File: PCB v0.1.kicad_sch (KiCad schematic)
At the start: 59 parts, among them J1 XT60 M (Vertical), J10 2.54mm 3P, J11 2.54mm 3P, J12 2.54mm 3P, J13 JST-SH 3P, J14 JST-SH 3P, J15 JST-SH 3P, J16 JST-SH 3P, J17 JST-SH 3P, J18 JST-SH 3P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

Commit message: Rev A finished. docs made, BOM made.
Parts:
- U1: Taobao https://item.taobao.com/item.htm?id=535067252604&last_time=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 -> https://item.taobao.com/item.htm?id=635227665423&spm=a312a.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
- U2: Taobao https://item.taobao.com/item.htm?abbucket=6&id=562966932146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 -> https://item.taobao.com/item.htm?id=635227665423&spm=a312a.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
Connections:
- net BLDC_0: now also A1.14 (GPIO10); no longer A1.4 (GPIO2)
- net BLDC_1: now also A1.16 (GPIO12); no longer A1.6 (GPIO4)
- net BLDC_2: now also A1.19 (GPIO14); no longer A1.9 (GPIO6)
- net BLDC_4: now also A1.32 (GPIO27_ADC1); no longer A1.14 (GPIO10)
- net BLDC_5: now also A1.26 (GPIO20); no longer A1.16 (GPIO12)
- net ENC_0: now also A1.4 (GPIO2); no longer A1.21 (GPIO16)
- net ENC_1: now also A1.5 (GPIO3); no longer A1.22 (GPIO17)
- net ENC_2: now also A1.6 (GPIO4); no longer A1.24 (GPIO18)
- net ENC_3: now also A1.7 (GPIO5); no longer A1.25 (GPIO19)
- net ENC_4: now also A1.9 (GPIO6); no longer A1.26 (GPIO20)
- net ENC_5: now also A1.10 (GPIO7); no longer A1.27 (GPIO21)
- net REV_0: now also A1.15 (GPIO11); no longer A1.5 (GPIO3)
- net REV_1: now also A1.17 (GPIO13); no longer A1.7 (GPIO5)
- net REV_2: now also A1.20 (GPIO15); no longer A1.10 (GPIO7)
- net REV_4: now also A1.34 (GPIO28_ADC2); no longer A1.15 (GPIO11)
- net REV_5: now also A1.27 (GPIO21); no longer A1.17 (GPIO13)
- net SERVO_0: now also A1.21 (GPIO16); no longer A1.19 (GPIO14)
- net SERVO_1: now also A1.22 (GPIO17); no longer A1.20 (GPIO15)
- net SERVO_2: now also A1.24 (GPIO18); no longer A1.32 (GPIO27_ADC1)
- net SERVO_3: now also A1.25 (GPIO19); no longer A1.34 (GPIO28_ADC2)

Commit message: Created new layout, fixed XT30 polarity
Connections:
- net BLDC_0: now also A1.7 (GPIO5); no longer A1.14 (GPIO10)
- net BLDC_1: now also A1.14 (GPIO10); no longer A1.16 (GPIO12)
- net BLDC_2: now also A1.11 (GPIO8); no longer A1.19 (GPIO14)
- net BLDC_3: now also A1.9 (GPIO6); no longer A1.11 (GPIO8)
- net BLDC_4: now also A1.5 (GPIO3); no longer A1.32 (GPIO27_ADC1)
- net BLDC_5: now also A1.22 (GPIO17); no longer A1.26 (GPIO20)
- net ENC_0: now also A1.26 (GPIO20); no longer A1.4 (GPIO2)
- net ENC_1: now also A1.25 (GPIO19); no longer A1.5 (GPIO3)
- net ENC_2: now also A1.24 (GPIO18); no longer A1.6 (GPIO4)
- net ENC_3: now also A1.27 (GPIO21); no longer A1.7 (GPIO5)
- net ENC_4: now also A1.32 (GPIO27_ADC1); no longer A1.9 (GPIO6)
- net ENC_5: now also A1.34 (GPIO28_ADC2); no longer A1.10 (GPIO7)
- net REV_0: now also A1.6 (GPIO4); no longer A1.15 (GPIO11)
- net REV_1: now also A1.15 (GPIO11); no longer A1.17 (GPIO13)
- net REV_2: now also A1.12 (GPIO9); no longer A1.20 (GPIO15)
- net REV_3: now also A1.10 (GPIO7); no longer A1.12 (GPIO9)
- net REV_4: now also A1.4 (GPIO2); no longer A1.34 (GPIO28_ADC2)
- net REV_5: now also A1.21 (GPIO16); no longer A1.27 (GPIO21)
- net SERVO_0: now also A1.16 (GPIO12); no longer A1.21 (GPIO16)
- net SERVO_1: now also A1.17 (GPIO13); no longer A1.22 (GPIO17)
- net SERVO_2: now also A1.19 (GPIO14); no longer A1.24 (GPIO18)
- net SERVO_3: now also A1.20 (GPIO15); no longer A1.25 (GPIO19)
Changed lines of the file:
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@@
+		)
+	)
+	(label "BLDC_3"
+		(at 308.61 80.01 0)
+		(effects
+			(font
+				(size 1.27 1.27)
+			)
+			(justify left bottom)
 		)
 	)
@@
 		)
 	)
-	(label "REV_5"
-		(at 377.19 80.01 180)
-		(effects
-			(font
-				(size 1.27 1.27)
-			)
-			(justify right bottom)
-		)
-	)
 	(label "BLDC_3"
 		(at 347.98 160.02 180)
@@
 		)
 	)
-	(label "BLDC_4"
-		(at 377.19 95.25 180)
-		(effects
-			(font
-				(size 1.27 1.27)
-			)
-			(justify right bottom)
-		)
-	)
 	(label "PICO_EN"
 		(at 179.07 44.45 0)
@@
 		)
 	)
+	(label "REV_0"
+		(at 308.61 74.93 0)
+		(effects
+			(font
+				(size 1.27 1.27)
+			)
+			(justify left bottom)
+		)
+	)
 	(label "SERVO_1"
 		(at 218.44 191.77 0)
@@
 		)
 	)
-	(label "ENC_4"
-		(at 308.61 80.01 0)
+	(label "ENC_0"
+		(at 377.19 77.47 180)
+		(effects
+			(font
+				(size 1.27 1.27)
+			)
+			(justify right bottom)
+		)
+	)
+	(label "BLDC_0"
+		(at 308.61 77.47 0)
 		(effects
 			(font
@@
 		)
 	)
-	(label "ENC_5"
-		(at 308.61 82.55 0)
+	(label "REV_2"
+		(at 308.61 87.63 0)
 		(effects
 			(font
@@
 		)
 	)
-	(label "ENC_0"
-		(at 308.61 69.85 0)
-		(effects
-			(font
-				(size 1.27 1.27)
-			)
-			(justify left bottom)
-		)
-	)
-	(label "REV_1"
-		(at 308.61 97.79 0)
-		(effects
-			(font
-				(size 1.27 1.27)
-			)
-			(justify left bottom)
-		)
-	)
-	(label "BLDC_1"
-		(at 308.61 95.25 0)
-		(effects
-			(font
-				(size 1.27 1.27)
-			)
-			(justify left bottom)
-		)
-	)
-	(label "BLDC_3"
-		(at 308.61 85.09 0)
+	(label "SERVO_2"
+		(at 308.61 100.33 0)
+		(effects
+			(font
+				(size 1.27 1.27)
+			)
+			(justify left bottom)
+		)
+	)
+	(label "REV_3"
+		(at 308.61 82.55 0)
+		(effects
+			(font
+				(size 1.27 1.27)
+			)
+			(justify left bottom)
+		)
+	)
+	(label "SERVO_3"
+		(at 308.61 102.87 0)
 		(effects
 			(font
@@
 		)
 	)
+	(label "ENC_3"
+		(at 377.19 80.01 180)
+		(effects
+			(font
+				(size 1.27 1.27)
+			)
+			(justify right bottom)
+		)
+	)
 	(label "DC Motors"
 		(at 256.54 133.35 0)
@@
 		)
 	)
+	(label "REV_1"
+		(at 308.61 92.71 0)
+		(effects
+			(font
+				(size 1.27 1.27)
+			)
+			(justify left bottom)
+		)
+	)
 	(label "22.2V to 12V"
 		(at 17.78 77.47 0)
@@
 		)
 	)
+	(label "SERVO_0"
+		(at 308.61 95.25 0)
+		(effects
+			(font
+				(size 1.27 1.27)
+			)
+			(justify left bottom)
+		)
+	)
 	(label "Battery Input"
 		(at 16.51 19.05 0)
@@
 		)
 	)
-	(label "REV_2"
-		(at 308.61 102.87 0)
-		(effects
-			(font
-				(size 1.27 1.27)
-			)
-			(justify left bottom)
-		)
-	)
 	(label "22.2V to 7.5V"
 		(at 87.63 77.47 0)
@@
 		)
 	)
-	(label "BLDC_5"
-		(at 377.19 77.47 180)
-		(effects
-			(font
-				(size 1.27 1.27)
-			)
-			(justify right bottom)
-		)
-	)
 	(label "REV_5"
 		(at 392.43 162.56 180)
@@
 		)
 	)
+	(label "BLDC_5"
+		(at 377.19 69.85 180)
+		(effects
+			(font
+				(size 1.27 1.27)
+			)
+			(justify right bottom)
+		)
+	)
+	(label "BLDC_4"
+		(at 308.61 72.39 0)
+		(effects
+			(font
+				(size 1.27 1.27)
+			)
+			(justify left bottom)
+		)
+	)
 	(label "ADC_IN"
 		(at 377.19 92.71 180)
@@
 		)
 	)
-	(label "SERVO_3"
-		(at 377.19 74.93 180)
-		(effects
-			(font
-				(size 1.27 1.27)
-			)
-			(justify right bottom)
-		)
-	)
 	(label "ADC_IN"
 		(at 237.49 152.4 180)
@@
 		)
 	)
-	(label "ENC_2"
-		(at 308.61 74.93 0)
-		(effects
-			(font
-				(size 1.27 1.27)
-			)
-			(justify left bottom)
-		)
-	)
-	(label "REV_3"
-		(at 308.61 87.63 0)
-		(effects
-			(font
-				(size 1.27 1.27)
-			)
-			(justify left bottom)
-		)
-	)
 	(label "SERVO_3"
 		(at 217.17 222.25 0)
@@
 		)
 	)
-	(label "SERVO_1"
-		(at 377.19 69.85 180)
-		(effects
-			(font
-				(size 1.27 1.27)
-			)
-			(justify right bottom)
-		)
-	)
-	(label "SERVO_2"
-		(at 377.19 72.39 180)
+	(label "BLDC_1"
+		(at 308.61 90.17 0)
+		(effects
+			(font
+				(size 1.27 1.27)
+			)
+			(justify left bottom)
+		)
+	)
+	(label "ENC_1"
+		(at 377.19 74.93 180)
 		(effects
 			(font
@@
 		)
 	)
-	(label "ENC_3"
-		(at 308.61 77.47 0)
-		(effects
-			(font
-				(size 1.27 1.27)
-			)
-			(justify left bottom)
-		)
-	)
 	(label "Raspberry Pi Pico 2"
 		(at 290.83 19.05 0)
@@
 		)
 	)
+	(label "SERVO_1"
+		(at 308.61 97.79 0)
+		(effects
+			(font
+				(size 1.27 1.27)
+			)
+			(justify left bottom)
+		)
+	)
+	(label "REV_4"
+		(at 308.61 69.85 0)
+		(effects
+			(font
+				(size 1.27 1.27)
+			)
+			(justify left bottom)
+		)
+	)
+	(label "ENC_4"
+		(at 377.19 95.25 180)
+		(effects
+			(font
+				(size 1.27 1.27)
+			)
+			(justify right bottom)
+		)
+	)
 	(label "PICO_INT"
 		(at 179.07 46.99 0)
@@
 		)
 	)
-	(label "ENC_1"
-		(at 308.61 72.39 0)
-		(effects
-			(font
-				(size 1.27 1.27)
-			)
-			(justify left bottom)
-		)
-	)
-	(label "BLDC_2"
-		(at 308.61 100.33 0)
-		(effects
-			(font
-				(size 1.27 1.27)
-			)
-			(justify left bottom)
-		)
-	)
-	(label "SERVO_0"
-		(at 377.19 67.31 180)
-		(effects
-			(font
-				(size 1.27 1.27)
-			)
-			(justify right bottom)
-		)
-	)
-	(label "BLDC_0"
-		(at 308.61 90.17 0)
-		(effects
-			(font
-				(size 1.27 1.27)
-			)
-			(justify left bottom)
+	(label "ENC_5"
+		(at 377.19 97.79 180)
+		(effects
+			(font
+				(size 1.27 1.27)
+			)
+			(justify right bottom)
 		)
 	)
@@
 		)
 	)
-	(label "REV_4"
-		(at 377.19 97.79 180)
-		(effects
-			(font
-				(size 1.27 1.27)
-			)
-			(justify right bottom)
-		)
-	)
-	(label "REV_0"
-		(at 308.61 92.71 0)
-		(effects
-			(font
-				(size 1.27 1.27)
-			)
-			(justify left bottom)
-		)
-	)
 	(label "REV_3"
 		(at 347.98 162.56 180)
@@
 		)
 	)
+	(label "REV_5"
+		(at 377.19 67.31 180)
+		(effects
+			(font
+				(size 1.27 1.27)
+			)
+			(justify right bottom)
+		)
+	)
+	(label "ENC_2"
+		(at 377.19 72.39 180)
+		(effects
+			(font
+				(size 1.27 1.27)
+			)
+			(justify right bottom)
+		)
+	)
 	(label "SERVO_0"
 		(at 179.07 191.77 0)
@@
 		(effects
 			(font
+				(size 1.27 1.27)
+			)
+			(justify left bottom)
+		)
+	)
+	(label "BLDC_2"
+		(at 308.61 85.09 0)
+		(effects
+			(font

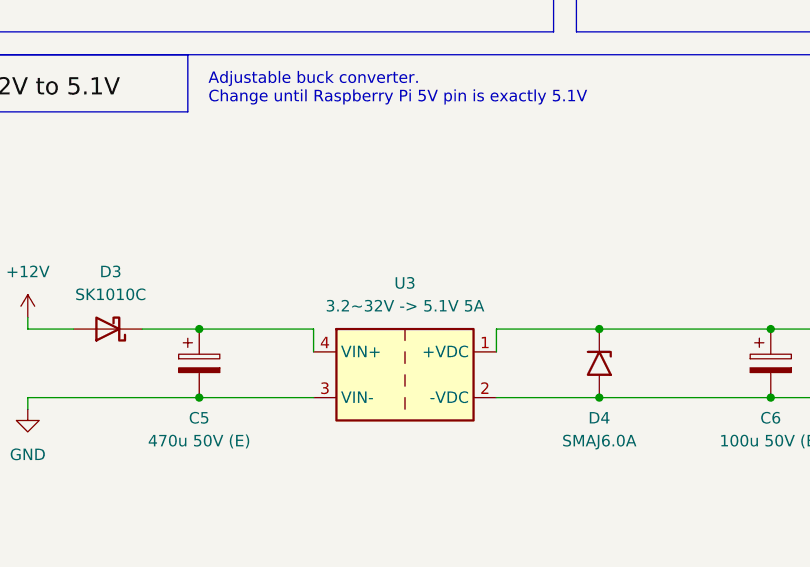
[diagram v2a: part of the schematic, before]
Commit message: v0.2. Corrected XT30 polarity, less than 10x10cm in size
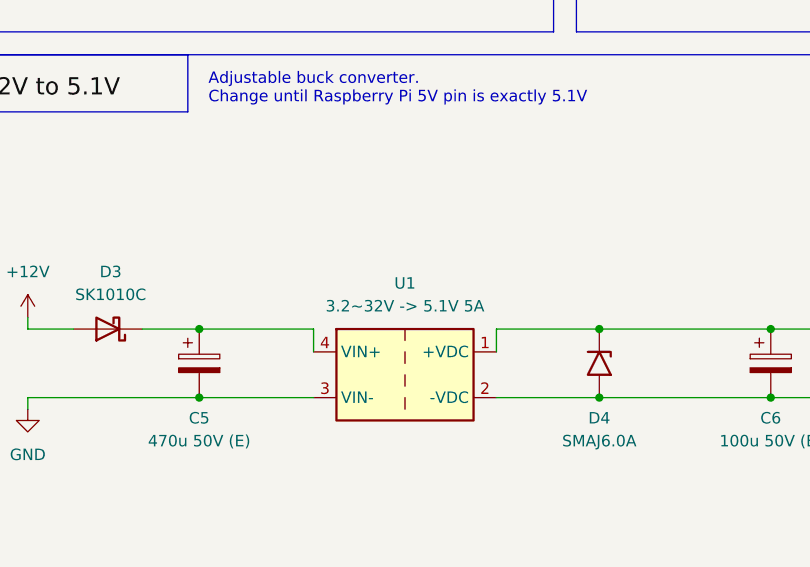
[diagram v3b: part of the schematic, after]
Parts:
- renumbered U3 to U1
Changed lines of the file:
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@@
 		(dnp no)
 		(fields_autoplaced yes)
-		(property "Reference" "U3"
+		(property "Reference" "U1"
 			(at 64.77 181.61 0)
 			(show_name no)
@@
 			(project "PCB v0.1"
 				(path "/4a9ac192-968f-45b6-b822-e3973cb892fb"
-					(reference "U3")
+					(reference "U1")
 					(unit 1)
 				)
